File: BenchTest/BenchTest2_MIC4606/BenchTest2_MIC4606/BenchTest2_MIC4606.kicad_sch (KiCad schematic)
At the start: 16 parts, among them J10 Conn_01x01_Socket, J11 Conn_01x01_Socket, J12 Conn_01x01_Socket, J13 Conn_01x01_Socket, J14 Conn_01x01_Socket, J15 Conn_01x01_Socket, J9 Conn_01x02_Socket

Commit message: WIP New Motor Design
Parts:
- removed C10, C12: 0.1u, Capacitor_SMD:C_0402_1005Metric_Pad0.74x0.62mm_HandSolder, symbol Device:C
- removed C11, C13: 2.2u, Capacitor_SMD:C_0603_1608Metric_Pad1.08x0.95mm_HandSolder, symbol Device:C
- removed J10, J11, J12, J13, J14, J15: Conn_01x01_Socket, Connector_PinHeader_2.54mm:PinHeader_1x01_P2.54mm_Vertical, symbol Connector:Conn_01x01_Socket
- removed J9: Conn_01x02_Socket, Connector_PinHeader_2.54mm:PinHeader_1x02_P2.54mm_Vertical, symbol Connector:Conn_01x02_Socket
- removed R12, R13, R14: 33, Resistor_SMD:R_0402_1005Metric_Pad0.72x0.64mm_HandSolder, symbol Device:R
- removed U2, U3: ~, Package_SO:SOIC-8_3.9x4.9mm_P1.27mm, symbol New_Library:FAN3217
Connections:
- no-connect marks 2 -> 0
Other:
- added sheet Armateur (Armateur.kicad_sch)
- added sheet MotorConnection (MotorConnection .kicad_sch)
- added sheet Regen (Regen.kicad_sch)

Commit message: WIP - Further refinement
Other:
- sheet Armateur ports: added ARM_DRV, MOT-, VBAT-, VDRIVE; removed none
- sheet Regen ports: added MOT-, REG_DRV, VBAT+, VDRIVE; removed none
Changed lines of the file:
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@@
+			)
+		)
+		(pin "ARM_DRV" input
+			(at 91.44 76.2 0)
+			(effects
+				(font
+					(size 1.27 1.27)
+				)
+				(justify right)
+			)
+		)
+		(pin "MOT-" input
+			(at 62.23 87.63 180)
+			(effects
+				(font
+					(size 1.27 1.27)
+				)
+				(justify left)
+			)
+		)
+		(pin "VBAT-" input
+			(at 91.44 100.33 0)
+			(effects
+				(font
+					(size 1.27 1.27)
+				)
+				(justify right)
+			)
+		)
+		(pin "VDRIVE" input
+			(at 91.44 81.28 0)
+			(effects
+				(font
+					(size 1.27 1.27)
+				)
+				(justify right)
 			)
 		)
@@
 			)
 		)
+		(pin "MOT-" input
+			(at 60.96 123.19 180)
+			(effects
+				(font
+					(size 1.27 1.27)
+				)
+				(justify left)
+			)
+		)
+		(pin "REG_DRV" input
+			(at 91.44 110.49 0)
+			(effects
+				(font
+					(size 1.27 1.27)
+				)
+				(justify right)
+			)
+		)
+		(pin "VBAT+" input
+			(at 91.44 137.16 0)
+			(effects
+				(font
+					(size 1.27 1.27)
+				)
+				(justify right)
+			)
+		)
+		(pin "VDRIVE" input
+			(at 91.44 114.3 0)
+			(effects
+				(font
+					(size 1.27 1.27)
+				)
+				(justify right)
+			)
+		)

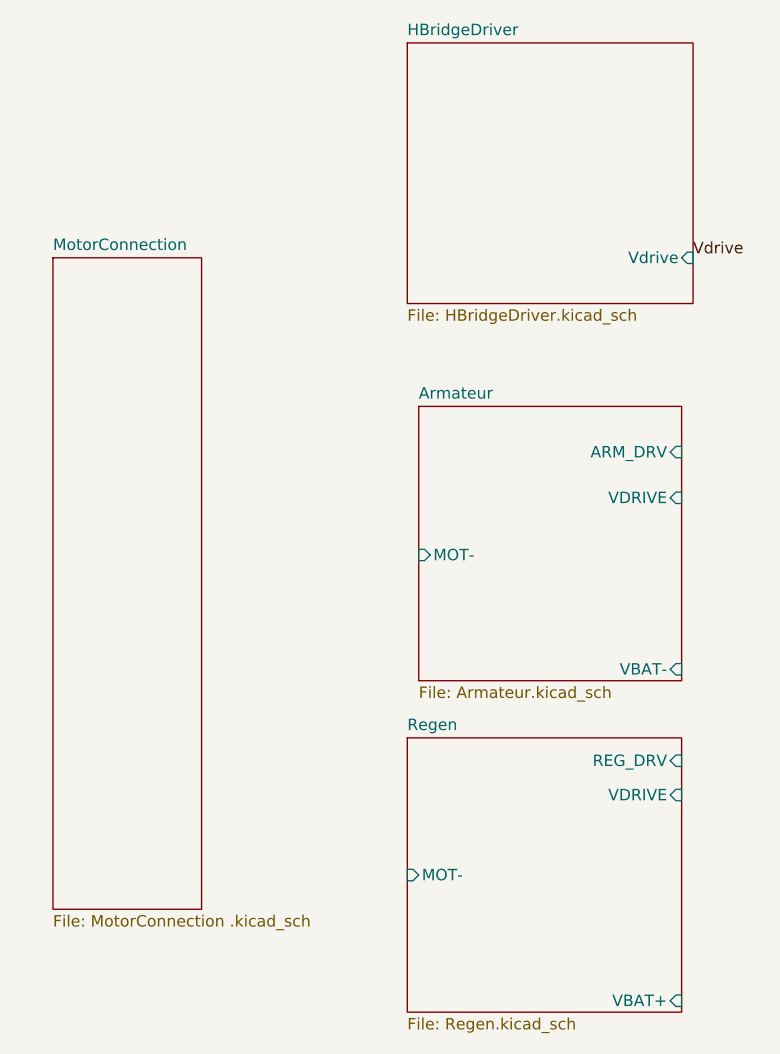
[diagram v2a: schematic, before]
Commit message: Defined Some parts, added notes for Arm/regen/H bridge
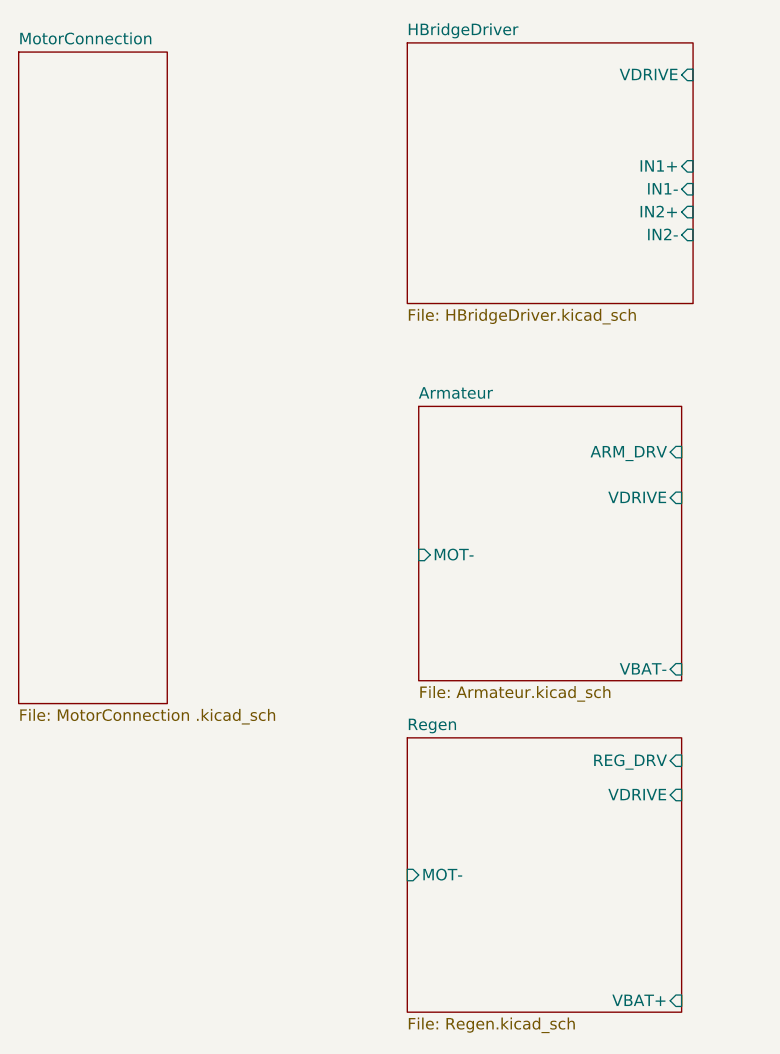
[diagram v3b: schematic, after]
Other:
- sheet HBridgeDriver ports: added IN1+, IN1-, IN2+, IN2-, VDRIVE; removed Vdrive
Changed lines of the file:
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@@
 	(generator_version "9.0")
 	(paper "A4")
-	(label "Vdrive"
-		(at 92.71 54.61 0)
-		(effects
-			(font
-				(size 1.27 1.27)
-			)
-			(justify left bottom)
-		)
-	)
 	(sheet
-		(at 21.59 54.61)
+		(at 17.78 31.75)
 		(size 16.51 72.39)
 		(exclude_from_sim no)
@@
 		)
 		(property "Sheetname" "MotorConnection"
-			(at 21.59 53.8984 0)
+			(at 17.78 31.0384 0)
 			(effects
 				(font
@@
 		)
 		(property "Sheetfile" "MotorConnection .kicad_sch"
-			(at 21.59 127.5846 0)
+			(at 17.78 104.7246 0)
 			(effects
 				(font
@@
 			)
 		)
-		(pin "Vdrive" input
-			(at 92.71 54.61 0)
+		(pin "IN1+" input
+			(at 92.71 44.45 0)
 			(effects
 				(font
+					(size 1.27 1.27)
+				)
+				(justify right)
+			)
+		)
+		(pin "IN1-" input
+			(at 92.71 46.99 0)
+			(effects
+				(font
+					(size 1.27 1.27)
+				)
+				(justify right)
+			)
+		)
+		(pin "IN2+" input
+			(at 92.71 49.53 0)
+			(effects
+				(font
+					(size 1.27 1.27)
+				)
+				(justify right)
+			)
+		)
+		(pin "IN2-" input
+			(at 92.71 52.07 0)
+			(effects
+				(font
+					(size 1.27 1.27)
+				)
+				(justify right)
+			)
+		)
+		(pin "VDRIVE" input
+			(at 92.71 34.29 0)
+			(effects
+				(font

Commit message: Additional Documents / Routing
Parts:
- added J2: Conn_01x03, symbol Connector_Generic:Conn_01x03
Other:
- sheet HBridgeDriver ports: added F1, F2; removed none
- sheet MotorConnection ports: added F1, F2, MOTORCON+, MOTORCON-; removed none
- note added: "TODO add Hall sensor connector footprint TODO what drive voltage for these TODO what drive out? Is it a current? or voltage?"
- note added: "TODO do I make this a seperate board? I.e. all this board is, is battery / motor connections? And an additional logic board? All connections are already isolated to the gate drives"

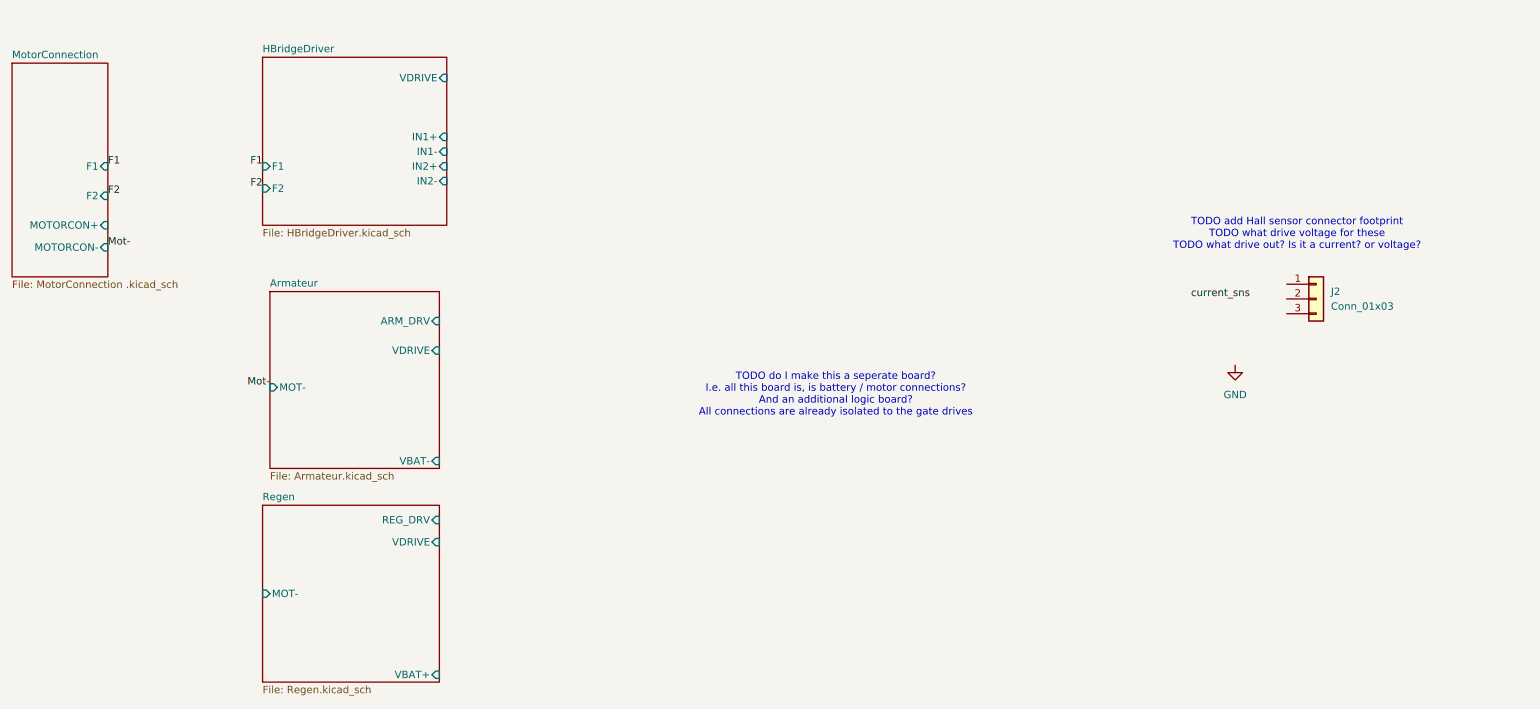
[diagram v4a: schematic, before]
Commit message: Continued Connections, split board design
Confirmed digital / motor board split
Configured Connections appropriately. Assigned some footprints.
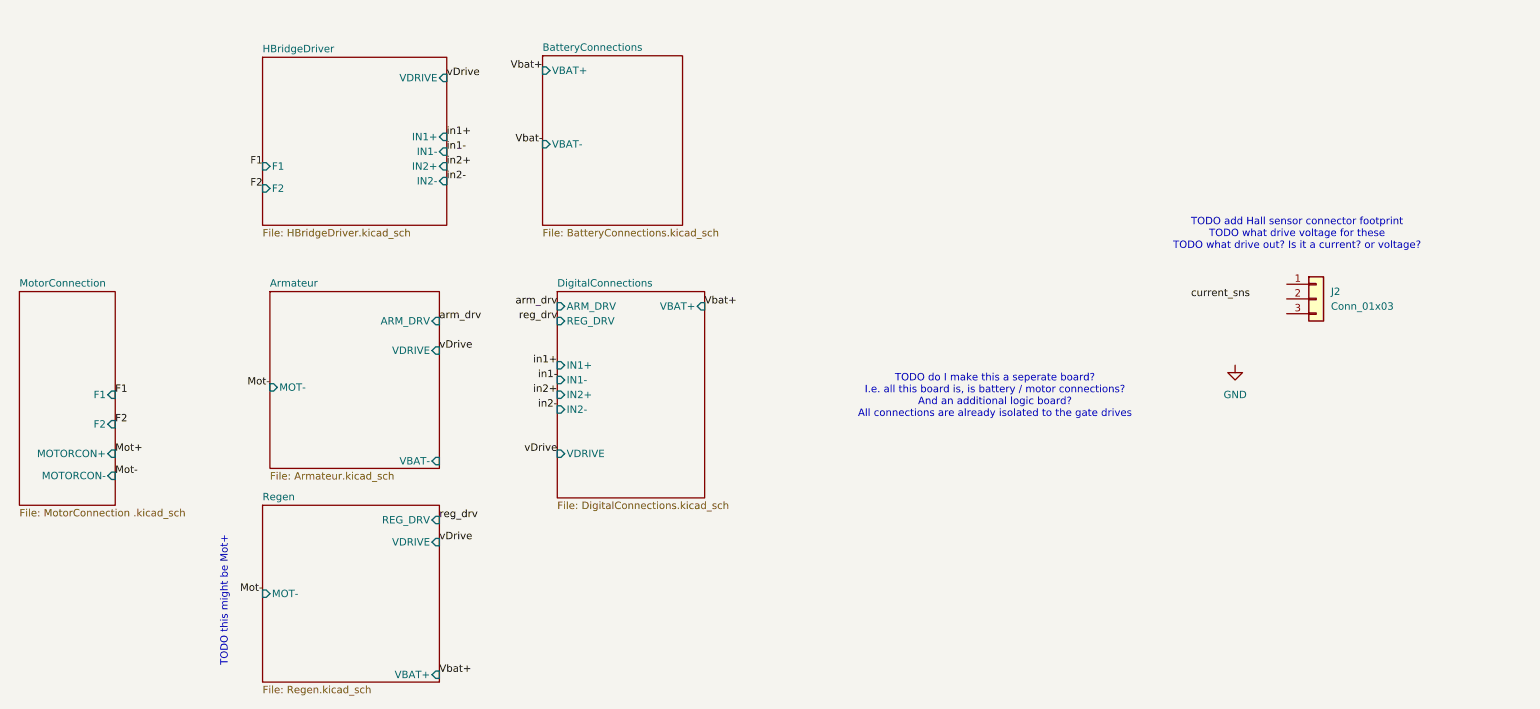
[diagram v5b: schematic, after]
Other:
- added sheet BatteryConnections (BatteryConnections.kicad_sch)
- added sheet DigitalConnections (DigitalConnections.kicad_sch)
- note added: "TODO this might be Mot+"

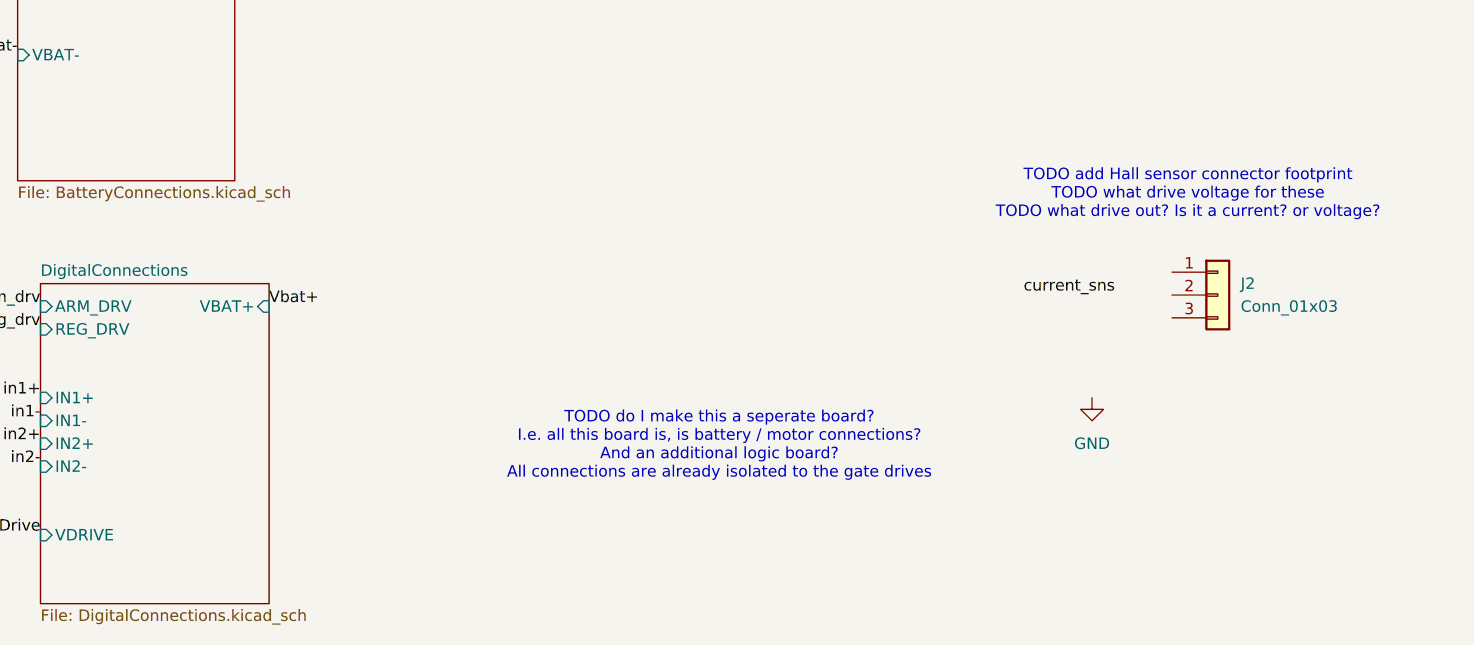
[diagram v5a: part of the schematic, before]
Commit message: Added motor voltage measurement for regen
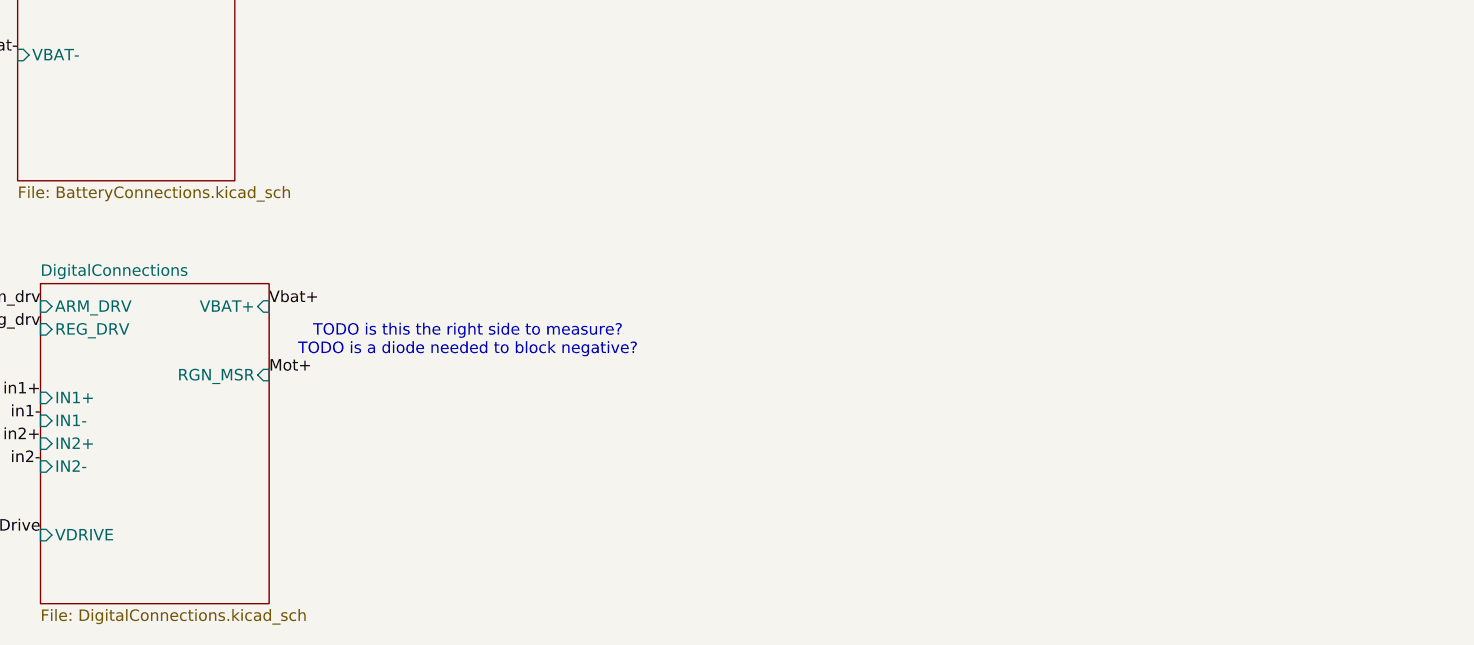
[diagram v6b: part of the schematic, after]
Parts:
- removed J2: Conn_01x03, symbol Connector_Generic:Conn_01x03
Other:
- sheet DigitalConnections ports: added RGN_MSR; removed none
- note added: "TODO is this the right side to measure? TODO is a diode needed to block negative?"
- note removed: "TODO add Hall sensor connector footprint TODO what drive voltage for these TODO what drive out? Is it a current? or voltage?"
- note removed: "TODO do I make this a seperate board? I.e. all this board is, is battery / motor connections? And an additional logic board? All connections are already isolated to the gate drives"
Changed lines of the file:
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@@
 	(generator_version "9.0")
 	(paper "A4")
-	(text "TODO add Hall sensor connector footprint\nTODO what drive voltage for these\nTODO what drive out? Is it a current? or voltage?"
-		(exclude_from_sim no)
-		(at 239.268 61.214 0)
-		(effects
-			(font
-				(size 1.27 1.27)
-			)
-		)
-	)
 	(text "TODO this might be Mot+"
 		(exclude_from_sim no)
@@
 		)
 	)
-	(text "TODO do I make this a seperate board?\nI.e. all this board is, is battery / motor connections?\nAnd an additional logic board? \nAll connections are already isolated to the gate drives"
+	(text "TODO is this the right side to measure?\nTODO is a diode needed to block negative?"
 		(exclude_from_sim no)
-		(at 187.198 89.154 0)
+		(at 159.258 77.47 0)
 		(effects
 			(font
@@
 		)
 	)
+	(label "Mot+"
+		(at 137.16 81.28 0)
+		(effects
+			(font
+				(size 1.27 1.27)
+			)
+			(justify left bottom)
+		)
+	)
 	(label "in1+"
 		(at 92.71 44.45 0)
@@
 		)
 	)
-	(label "current_sns"
-		(at 231.14 72.39 180)
-		(effects
-			(font
-				(size 1.27 1.27)
-			)
-			(justify right bottom)
-		)
-	)
 	(label "in1-"
 		(at 111.76 86.36 180)
@@
 			)
 			(justify right bottom)
-		)
-	)
-	(symbol
-		(lib_id "Connector_Generic:Conn_01x03")
-		(at 242.57 72.39 0)
-		(unit 1)
-		(exclude_from_sim no)
-		(in_bom yes)
-		(on_board yes)
-		(dnp no)
-		(fields_autoplaced yes)
-		(property "Reference" "J2"
-			(at 245.11 71.1199 0)
-			(effects
-				(font
-					(size 1.27 1.27)
-				)
-				(justify left)
-			)
-		)
-		(property "Value" "Conn_01x03"
-			(at 245.11 73.6599 0)
-			(effects
-				(font
-					(size 1.27 1.27)
-				)
-				(justify left)
-			)
-		)
-		(property "Footprint" ""
-			(at 242.57 72.39 0)
-			(effects
-				(font
-					(size 1.27 1.27)
-				)
-				(hide yes)
-			)
-		)
-		(property "Datasheet" "~"
-			(at 242.57 72.39 0)
-			(effects
-				(font
-					(size 1.27 1.27)
-				)
-				(hide yes)
-			)
-		)
-		(property "Description" "Generic connector, single row, 01x03, script generated (kicad-library-utils/schlib/autogen/connector/)"
-			(at 242.57 72.39 0)
-			(effects
-				(font
-					(size 1.27 1.27)
-				)
-				(hide yes)
-			)
-		)
-		(pin "1"
-		)
-		(pin "2"
-		)
-		(pin "3"
-		)
-		(instances
-			(project "BenchTest2_MIC4606"
-				(path "/5c5197d3-4aa5-4f8b-b790-1e4b8d49fd62"
-					(reference "J2")
-					(unit 1)
-				)
-			)
-		)
-	)
-	(symbol
-		(lib_id "power:GND")
-		(at 228.6 83.82 0)
-		(unit 1)
-		(exclude_from_sim no)
-		(in_bom yes)
-		(on_board yes)
-		(dnp no)
-		(fields_autoplaced yes)
-		(property "Reference" "#PWR01"
-			(at 228.6 90.17 0)
-			(effects
-				(font
-					(size 1.27 1.27)
-				)
-				(hide yes)
-			)
-		)
-		(property "Value" "GND"
-			(at 228.6 88.9 0)
-			(effects
-				(font
-					(size 1.27 1.27)
-				)
-			)
-		)
-		(property "Footprint" ""
-			(at 228.6 83.82 0)
-			(effects
-				(font
-					(size 1.27 1.27)
-				)
-				(hide yes)
-			)
-		)
-		(property "Datasheet" ""
-			(at 228.6 83.82 0)
-			(effects
-				(font
-					(size 1.27 1.27)
-				)
-				(hide yes)
-			)
-		)
-		(property "Description" "Power symbol creates a global label with name \"GND\" , ground"
-			(at 228.6 83.82 0)
-			(effects
-				(font
-					(size 1.27 1.27)
-				)
-				(hide yes)
-			)
-		)
-		(pin "1"
-		)
-		(instances
-			(project "BenchTest2_MIC4606"
-				(path "/5c5197d3-4aa5-4f8b-b790-1e4b8d49fd62"
-					(reference "#PWR01")
-					(unit 1)
-				)
-			)
 		)
 	)
@@
 			)
 		)
+		(pin "RGN_MSR" input
+			(at 137.16 81.28 0)
+			(effects
+				(font
+					(size 1.27 1.27)
+				)
+				(justify right)
+			)
+		)
